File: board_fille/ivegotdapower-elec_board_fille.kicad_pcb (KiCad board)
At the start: 2 copper layers, 44.5 x 20.3 mm, 16 parts, among them J1 Conn_02x03_Odd_Even, J2 Conn_02x03_Odd_Even, U1 LM2596S-ADJ

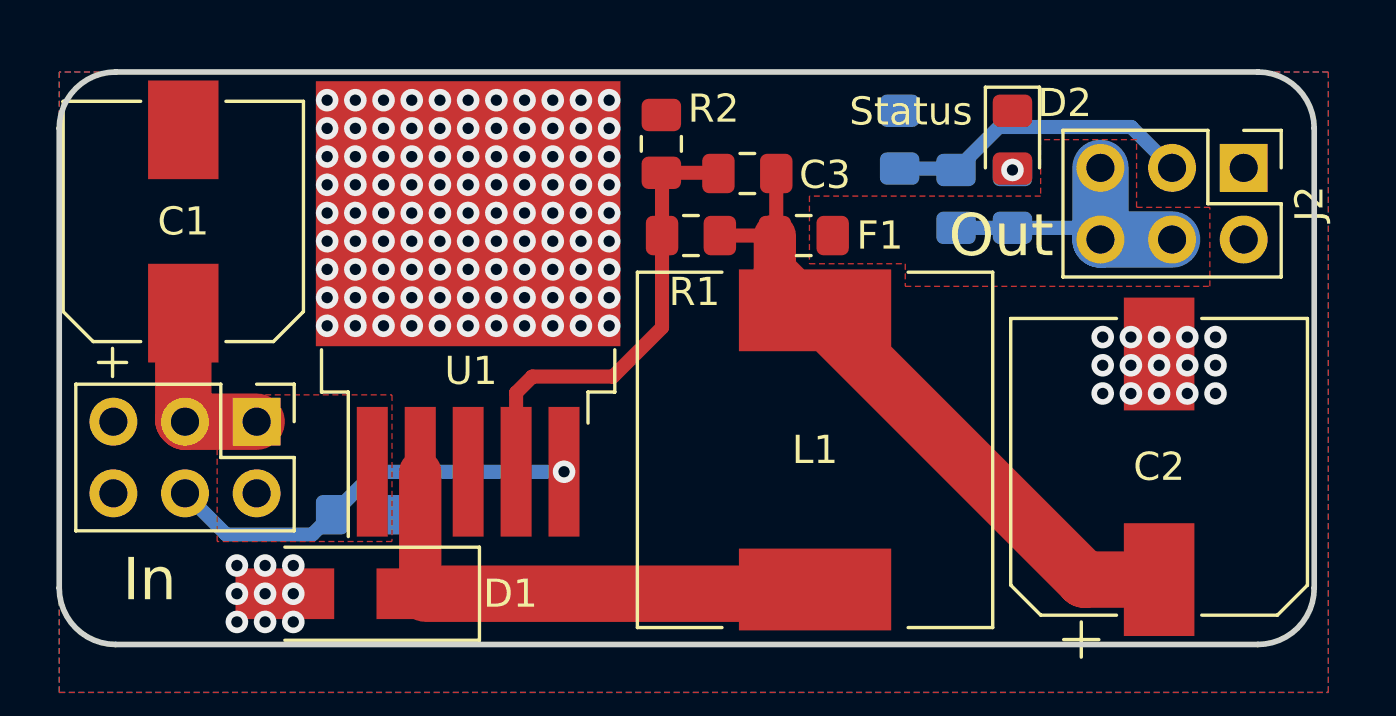
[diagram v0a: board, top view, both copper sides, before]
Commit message: Add potentiometer to board. Move SMD further apart.
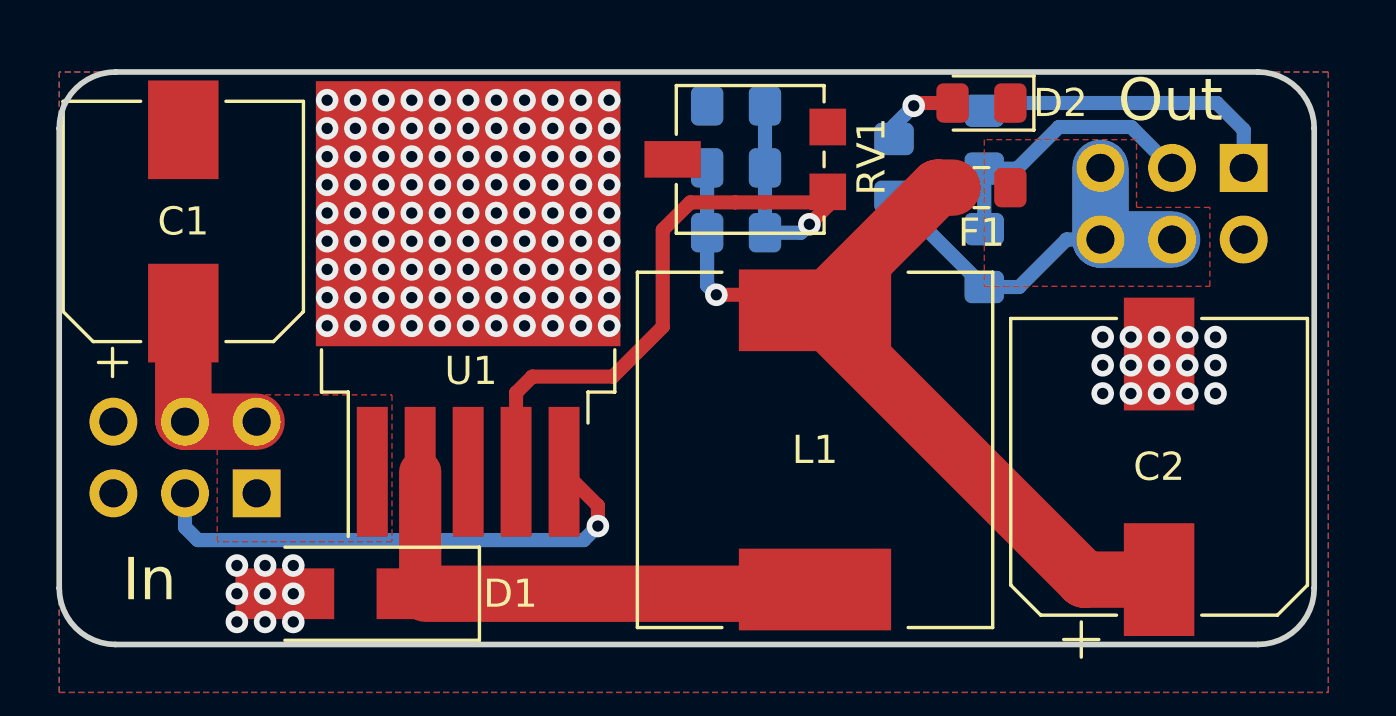
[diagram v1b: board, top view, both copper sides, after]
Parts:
- removed the R1 at (122.4, 105.8)
- removed R6: R, Resistor_SMD:R_0805_2012Metric_Pad1.15x1.40mm_HandSolder
- added R2: 3.1k, Resistor_SMD:R_0805_2012Metric_Pad1.15x1.40mm_HandSolder, B.Cu at (124.0, 105.7)
- added RV1: R_POT, Potentiometer_SMD:Potentiometer_Vishay_TS53YL_Vertical, F.Cu at (124.5, 103.1)
- C3, J1: moved to B.Cu
- J2: footprint Connector_PinHeader_2.54mm:PinHeader_2x03_P2.54mm_Vertical -> Connector_PinSocket_2.54mm:PinSocket_2x03_P2.54mm_Vertical; moved to B.Cu
- R1: renamed from R2; moved to B.Cu
- moved F1 6.53 mm to (132.7, 104.1)
- moved R3 4.34 mm to (129.6, 103.4)
- moved R5 3.00 mm to (132.8, 102.4)
- moved R1 2.97 mm to (124.0, 101.2), turned to 0 degrees
- moved J1 2.54 mm to (107.0, 114.9), turned to 90 degrees
- moved R4 2.33 mm to (132.8, 106.6)
- moved D2 1.70 mm to (132.7, 101.1), turned to 180 degrees
- moved C3 0.45 mm to (124.0, 103.4), turned to 0 degrees
- turned J2 to 90 degrees
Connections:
- J1 pad 3: /Power_Input -> /on-off
- J1 pad 4: /on-off -> /Power_Input
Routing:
- net GND: track 0.00 -> 11.1 mm
- net Net-(C3-Pad2): track 16.5 -> 26.4 mm, vias 0 -> 1
- net Net-(C2-Pad1): track 23.6 -> 31.3 mm, vias 0 -> 1
- net /on-off: track 15.0 -> 19.1 mm
- net /Power_Output: track 10.4 -> 14.4 mm
- net Net-(D2-Pad2): track 0.00 -> 2.88 mm
- net /voltage_measure: track 10.9 -> 10.0 mm
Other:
- board text removed: "Status"

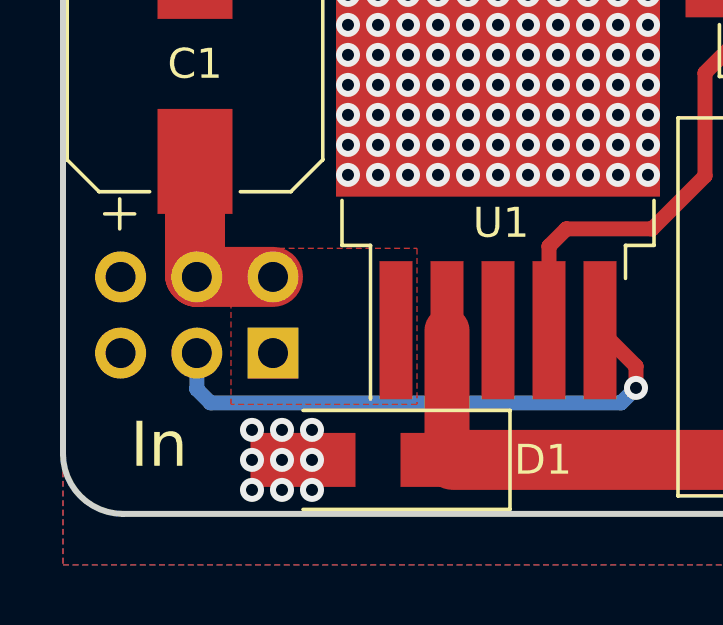
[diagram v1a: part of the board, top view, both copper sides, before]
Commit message: add text below pcb
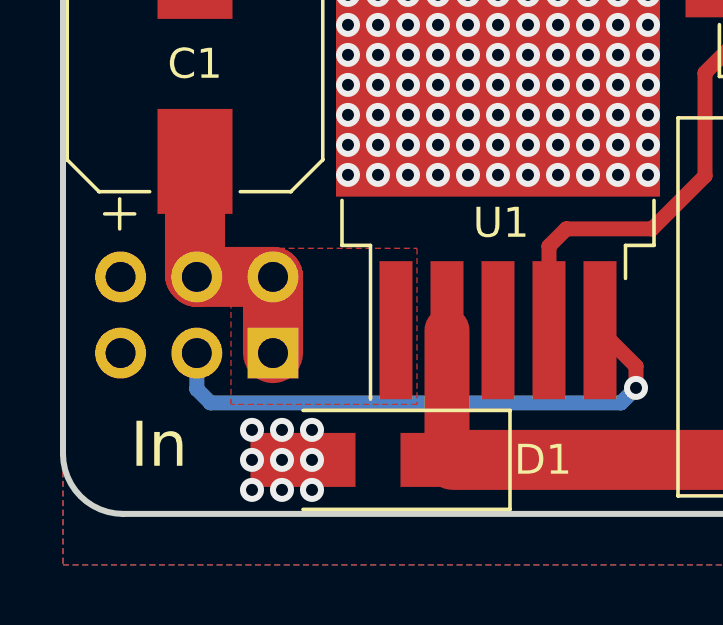
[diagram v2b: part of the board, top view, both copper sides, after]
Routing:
- net /Power_Input: track 6.41 -> 8.95 mm
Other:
- board text added: "Connect either RV1 or R2. Vout = 1.23 × (1+R1/R2)"

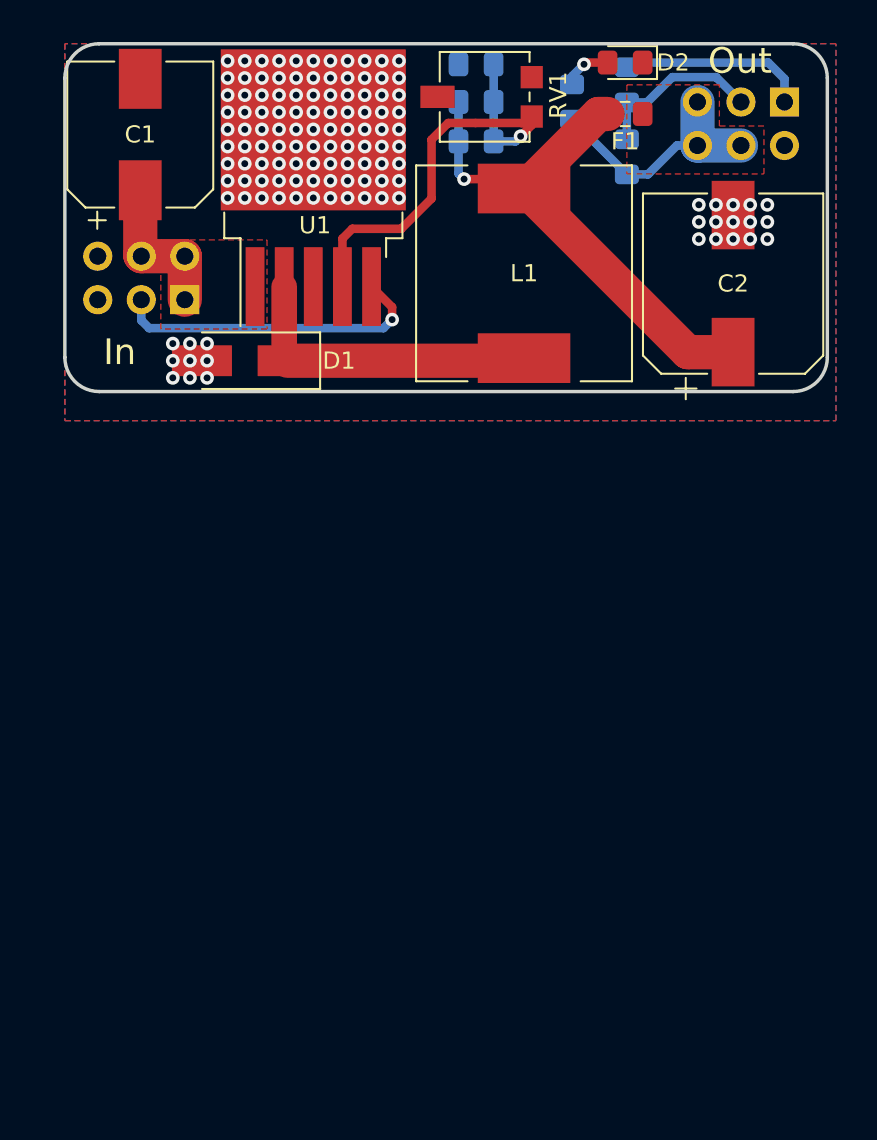
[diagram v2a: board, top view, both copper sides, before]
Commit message: Add possible variant for board fille
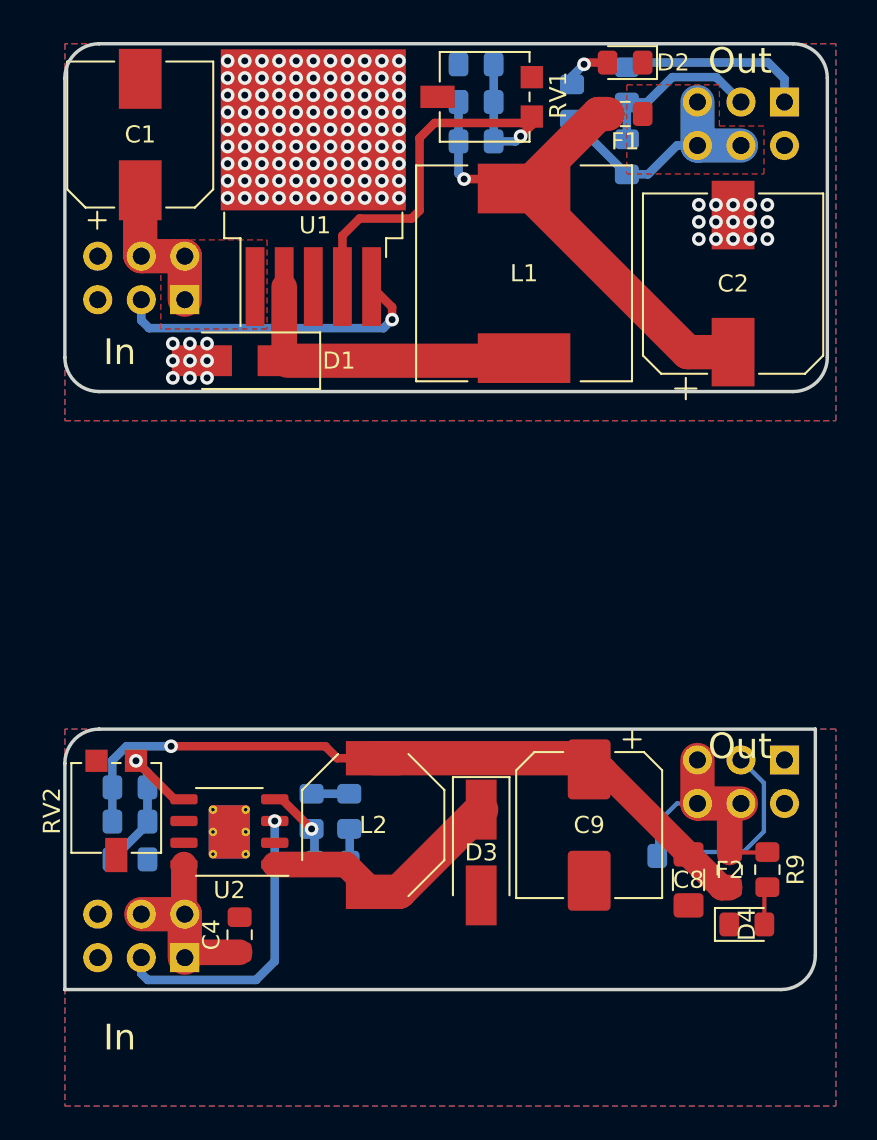
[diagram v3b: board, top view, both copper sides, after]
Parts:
- added C4: 10uF, Capacitor_SMD:C_0805_2012Metric_Pad1.15x1.40mm_HandSolder, F.Cu at (110.2, 152.0)
- added C5: 22nF, Capacitor_SMD:C_0805_2012Metric_Pad1.15x1.40mm_HandSolder, B.Cu at (115.6, 147.8)
- added C6: 220pF, Capacitor_SMD:C_0805_2012Metric_Pad1.15x1.40mm_HandSolder, B.Cu at (114.4, 144.8)
- added C7: 15nF, Capacitor_SMD:C_0805_2012Metric_Pad1.15x1.40mm_HandSolder, B.Cu at (103.8, 143.4)
- added C8: C, Capacitor_SMD:C_1206_3216Metric_Pad1.42x1.75mm_HandSolder, F.Cu at (136.4, 148.8)
- added C9: 330uF, Capacitor_SMD:CP_Elec_8x10, F.Cu at (130.6, 145.6)
- added D3: D_Schottky 3A 40V, Diode_SMD:D_SMA_Handsoldering, F.Cu at (124.3, 147.2)
- added D4: LED, LED_SMD:LED_0805_2012Metric_Pad1.15x1.40mm_HandSolder, F.Cu at (139.8, 151.4)
- added F2: Fuse, Fuse:Fuse_0805_2012Metric_Pad1.15x1.40mm_HandSolder, F.Cu at (138.8, 148.2)
- added J3: Conn_02x03_Odd_Even, Connector_PinHeader_2.54mm:PinHeader_2x03_P2.54mm_Vertical, B.Cu at (107.0, 153.3)
- added J4: Conn_02x03_Odd_Even, Connector_PinSocket_2.54mm:PinSocket_2x03_P2.54mm_Vertical, B.Cu at (142.0, 141.8)
- added L2: 15uH, Inductor_SMD:L_Bourns-SRU8043, F.Cu at (118.0, 145.6)
- added R10: R, Resistor_SMD:R_0805_2012Metric_Pad1.15x1.40mm_HandSolder, B.Cu at (135.6, 147.4)
- added R11: R, Resistor_SMD:R_0805_2012Metric_Pad1.15x1.40mm_HandSolder, B.Cu at (138.8, 148.2)
- added R6: 4k7, Resistor_SMD:R_0805_2012Metric_Pad1.15x1.40mm_HandSolder, B.Cu at (116.6, 144.8)
- added R7: 1k, Resistor_SMD:R_0805_2012Metric_Pad1.15x1.40mm_HandSolder, B.Cu at (103.8, 147.6)
- added R8: 3.1k, Resistor_SMD:R_0805_2012Metric_Pad1.15x1.40mm_HandSolder, B.Cu at (103.8, 145.4)
- added R9: R, Resistor_SMD:R_0805_2012Metric_Pad1.15x1.40mm_HandSolder, F.Cu at (141.0, 148.2)
- added RV2: R_POT, Potentiometer_SMD:Potentiometer_Vishay_TS53YL_Vertical, F.Cu at (103.0, 144.6)
- added U2: L5973D, Package_SO:HSOP-8-1EP_3.9x4.9mm_P1.27mm_EP2.41x3.1mm_ThermalVias, F.Cu at (109.6, 146.0)
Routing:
- net Net-(C7-Pad1): track 0.00 -> 43.4 mm, vias 0 -> 1
- net /on-off: track 19.1 -> 36.6 mm, vias 1 -> 2
- net /Power_Output: track 14.4 -> 29.6 mm
- net Net-(D3-Pad1): track 0.00 -> 14.7 mm
- net /Power_Input: track 8.95 -> 20.3 mm
- net Net-(C7-Pad2): track 0.00 -> 10.6 mm, vias 0 -> 1
- net /voltage_measure: track 10.0 -> 19.5 mm
- net Net-(C5-Pad1): track 0.00 -> 4.67 mm, vias 0 -> 1
- net Net-(D4-Pad2): track 0.00 -> 2.25 mm
- net GND: track 11.1 -> 13.3 mm
- net Net-(C5-Pad2): track 0.00 -> 1.99 mm
- net Net-(C3-Pad2): track 26.4 -> 27.0 mm
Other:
- board size 44.5 x 20.3 mm -> 44.5 x 55.2 mm
